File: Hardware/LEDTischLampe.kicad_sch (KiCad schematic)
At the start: 33 parts, among them J1 Conn_01x02_Socket, J2 USB_C_Receptacle_USB2.0_14P, J3 Conn_02x03_Counter_Clockwise, Q1 P-CHANNEL-MOSFET, SW1 Reset, SW2 User, U1 ESP32-C3-WROOM-02, U7 RY8310

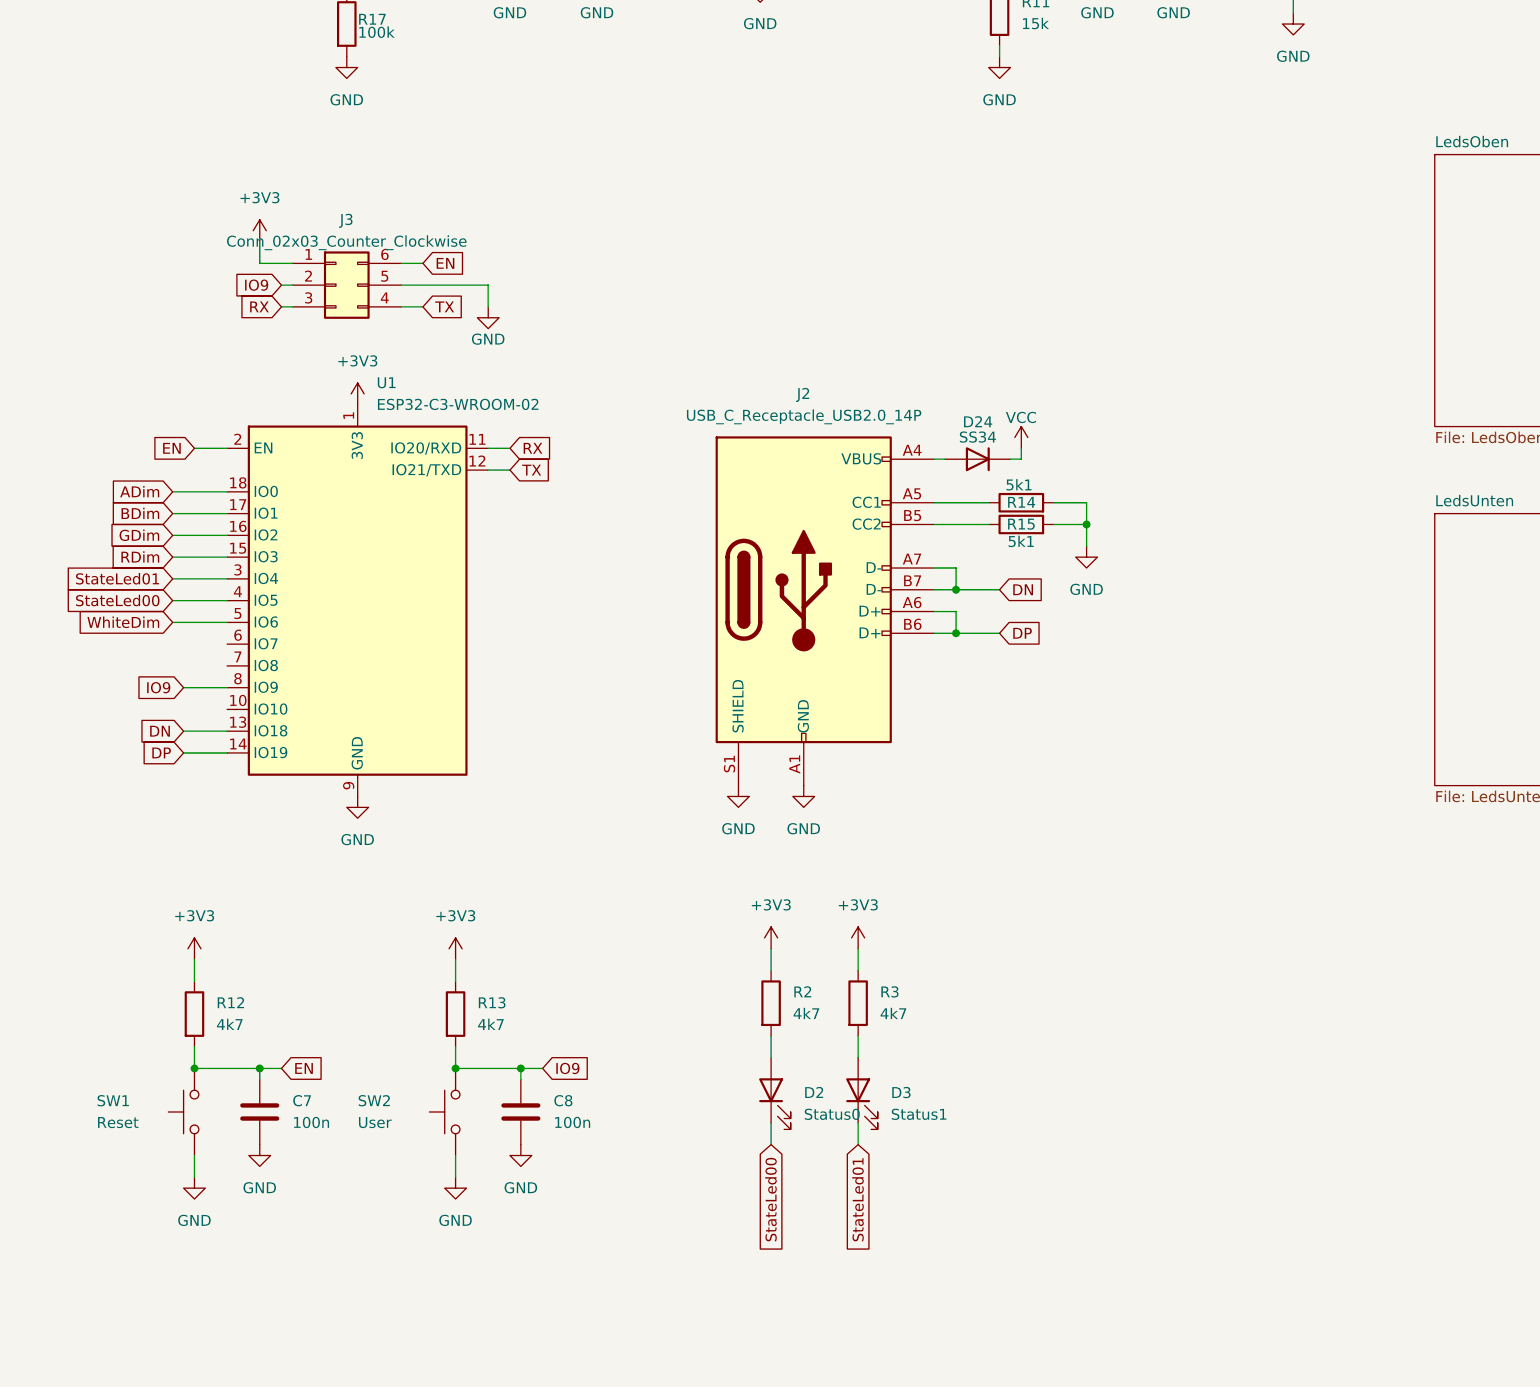
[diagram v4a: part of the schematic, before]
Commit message: some fixes and BOM optimization, heatsinking, etc
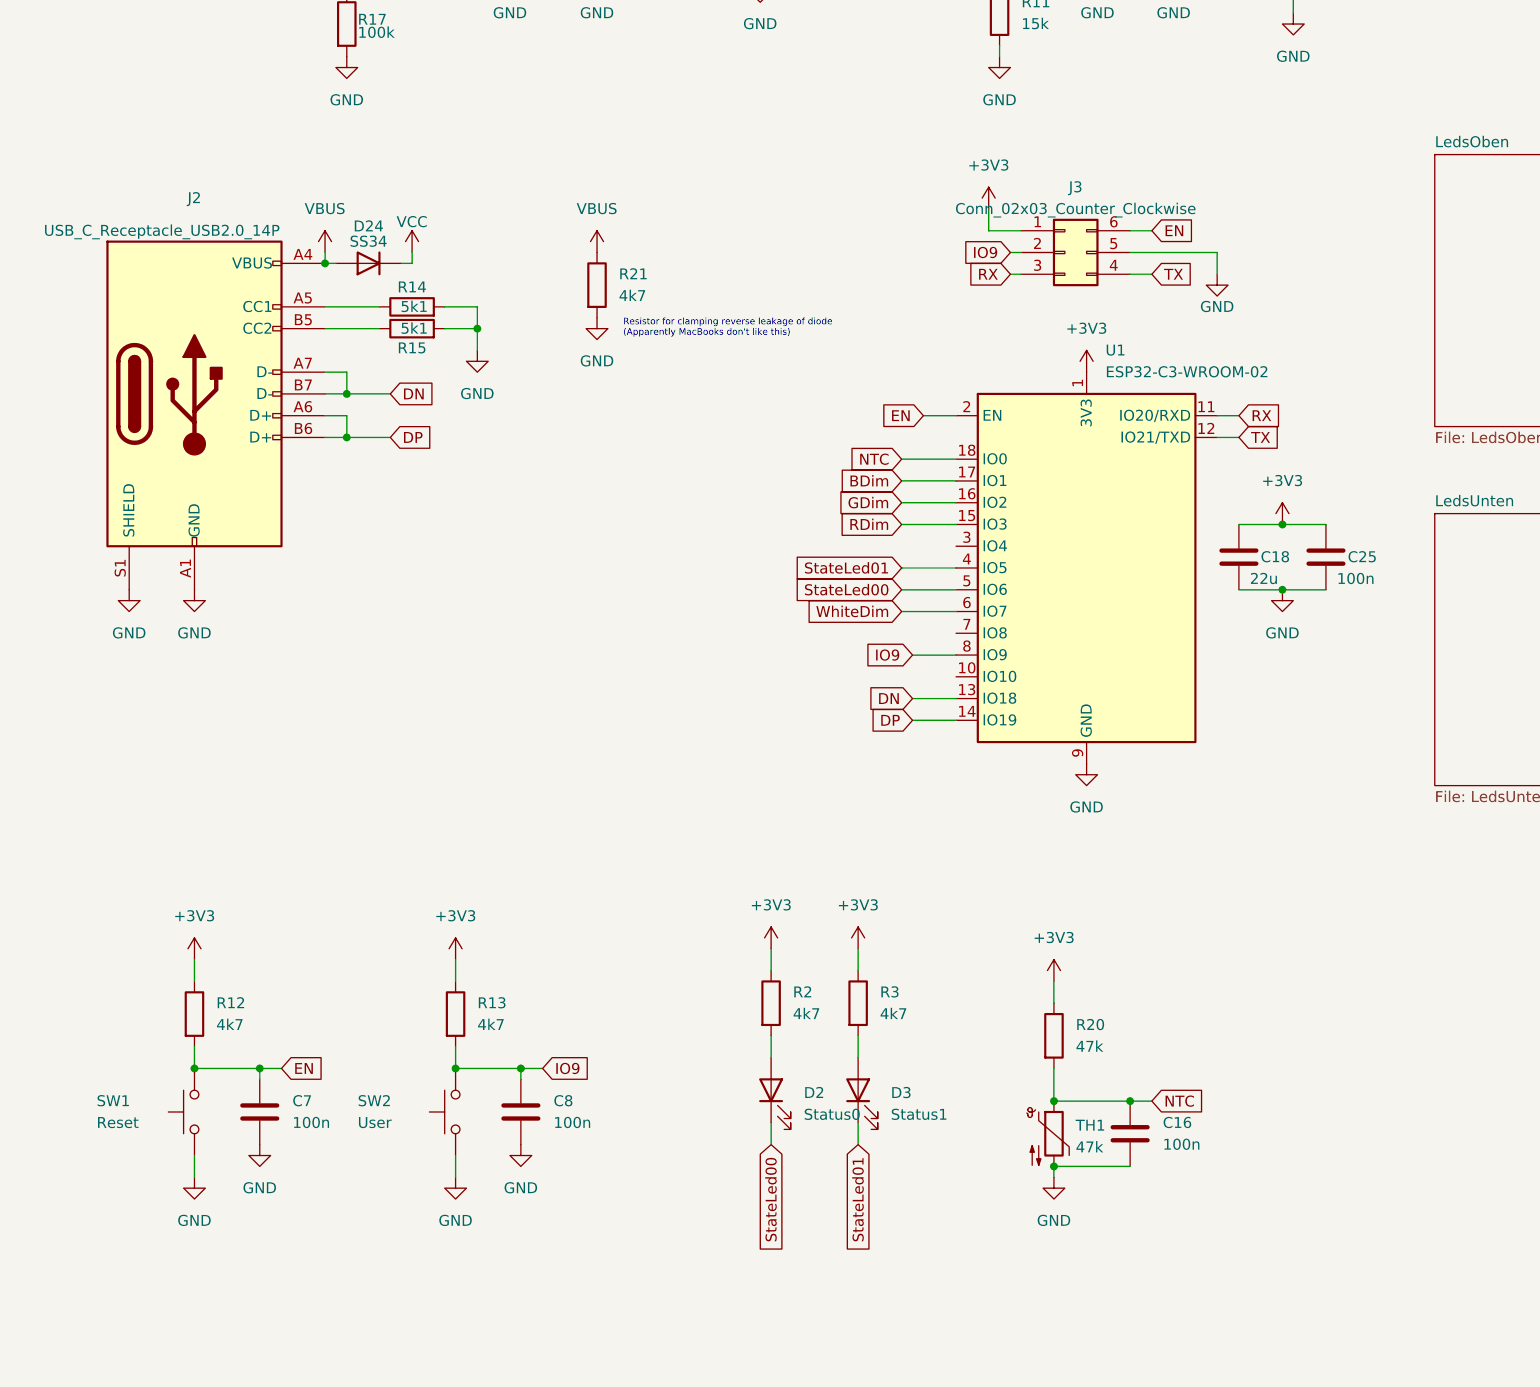
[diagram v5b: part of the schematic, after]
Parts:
- added C16, C25: 100n, Capacitor_SMD:C_0402_1005Metric, symbol Device:C
- added C18: 22u, Capacitor_SMD:C_1210_3225Metric, symbol Device:C
- added R20: 47k, Resistor_SMD:R_0402_1005Metric, symbol Device:R
- added R21: 4k7, Resistor_SMD:R_0402_1005Metric, symbol Device:R
- added TH1: 47k, Resistor_SMD:R_0402_1005Metric, symbol Device:Thermistor_NTC
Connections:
- net +3V3: now also C18.1, C25.1, R20.1
- net GND: now also C16.2, C18.2, C25.2, R21.2, TH1.2
- net StateLed00: now also U1.5 (IO6); no longer U1.4 (IO5)
- net StateLed01: now also U1.4 (IO5); no longer U1.3 (IO4)
- net WhiteDim: now also U1.6 (IO7); no longer U1.5 (IO6)
- net VBUS: now reaches D24.2 (A), J2.A4 (VBUS), J2.A9 (VBUS), J2.B4 (VBUS), J2.B9 (VBUS)
- net VBUS: now also R21.1
- net ADim renamed NTC
- net NTC: now also C16.1, R20.2, TH1.1
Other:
- note added: "Resistor for clamping reverse leakage of diode (Apparently MacBooks don't like this)"
- moved on the sheet: D24, J2, J3, R14, R15, U1

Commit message: final touches for v1.0
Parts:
- removed D34: 15V, Diode_SMD:D_0402_1005Metric, symbol Device:D_Zener
- removed Q1: P-CHANNEL-MOSFET, Package_SON:VSON-8_3.3x3.3mm_P0.65mm_NexFET, symbol Techbeard:P-CHANNEL-MOSFET
- removed R17: 100k, Resistor_SMD:R_0402_1005Metric, symbol Device:R
- added D25: SS34, Diode_SMD:D_SMA, symbol Device:D
- C1, C16, C25, C4, C5, C7, C8: LCSC C307331 -> (none)
- C18, C2, C6: footprint Capacitor_SMD:C_1210_3225Metric -> Capacitor_SMD:C_0805_2012Metric; LCSC C52306 -> (none)
- D1: LCSC C84256 -> (none)
- D2: LCSC C2296 -> (none)
- D24: LCSC C8678 -> (none)
- D3: LCSC C2297 -> (none)
- J2: LCSC C2927038 -> (none)
- L1: LCSC C5832376 -> (none)
- R1, R12, R13, R2, R20, R21, R3: LCSC C25900 -> (none)
- R10: LCSC C25792 -> (none)
- R11: LCSC C25756 -> (none)
- R14, R15: LCSC C25905 -> (none)
- SW1, SW2: LCSC C318884 -> (none)
- TH1: LCSC C2991699 -> (none)
- U1: LCSC C2934560 -> (none)
- U7: LCSC C370876 -> (none)
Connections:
- net GND: now also D25.2 (A)
- net VCC: now also J1.1 (Pin_1), D25.1 (K)
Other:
- note added: "Crowbar diode"

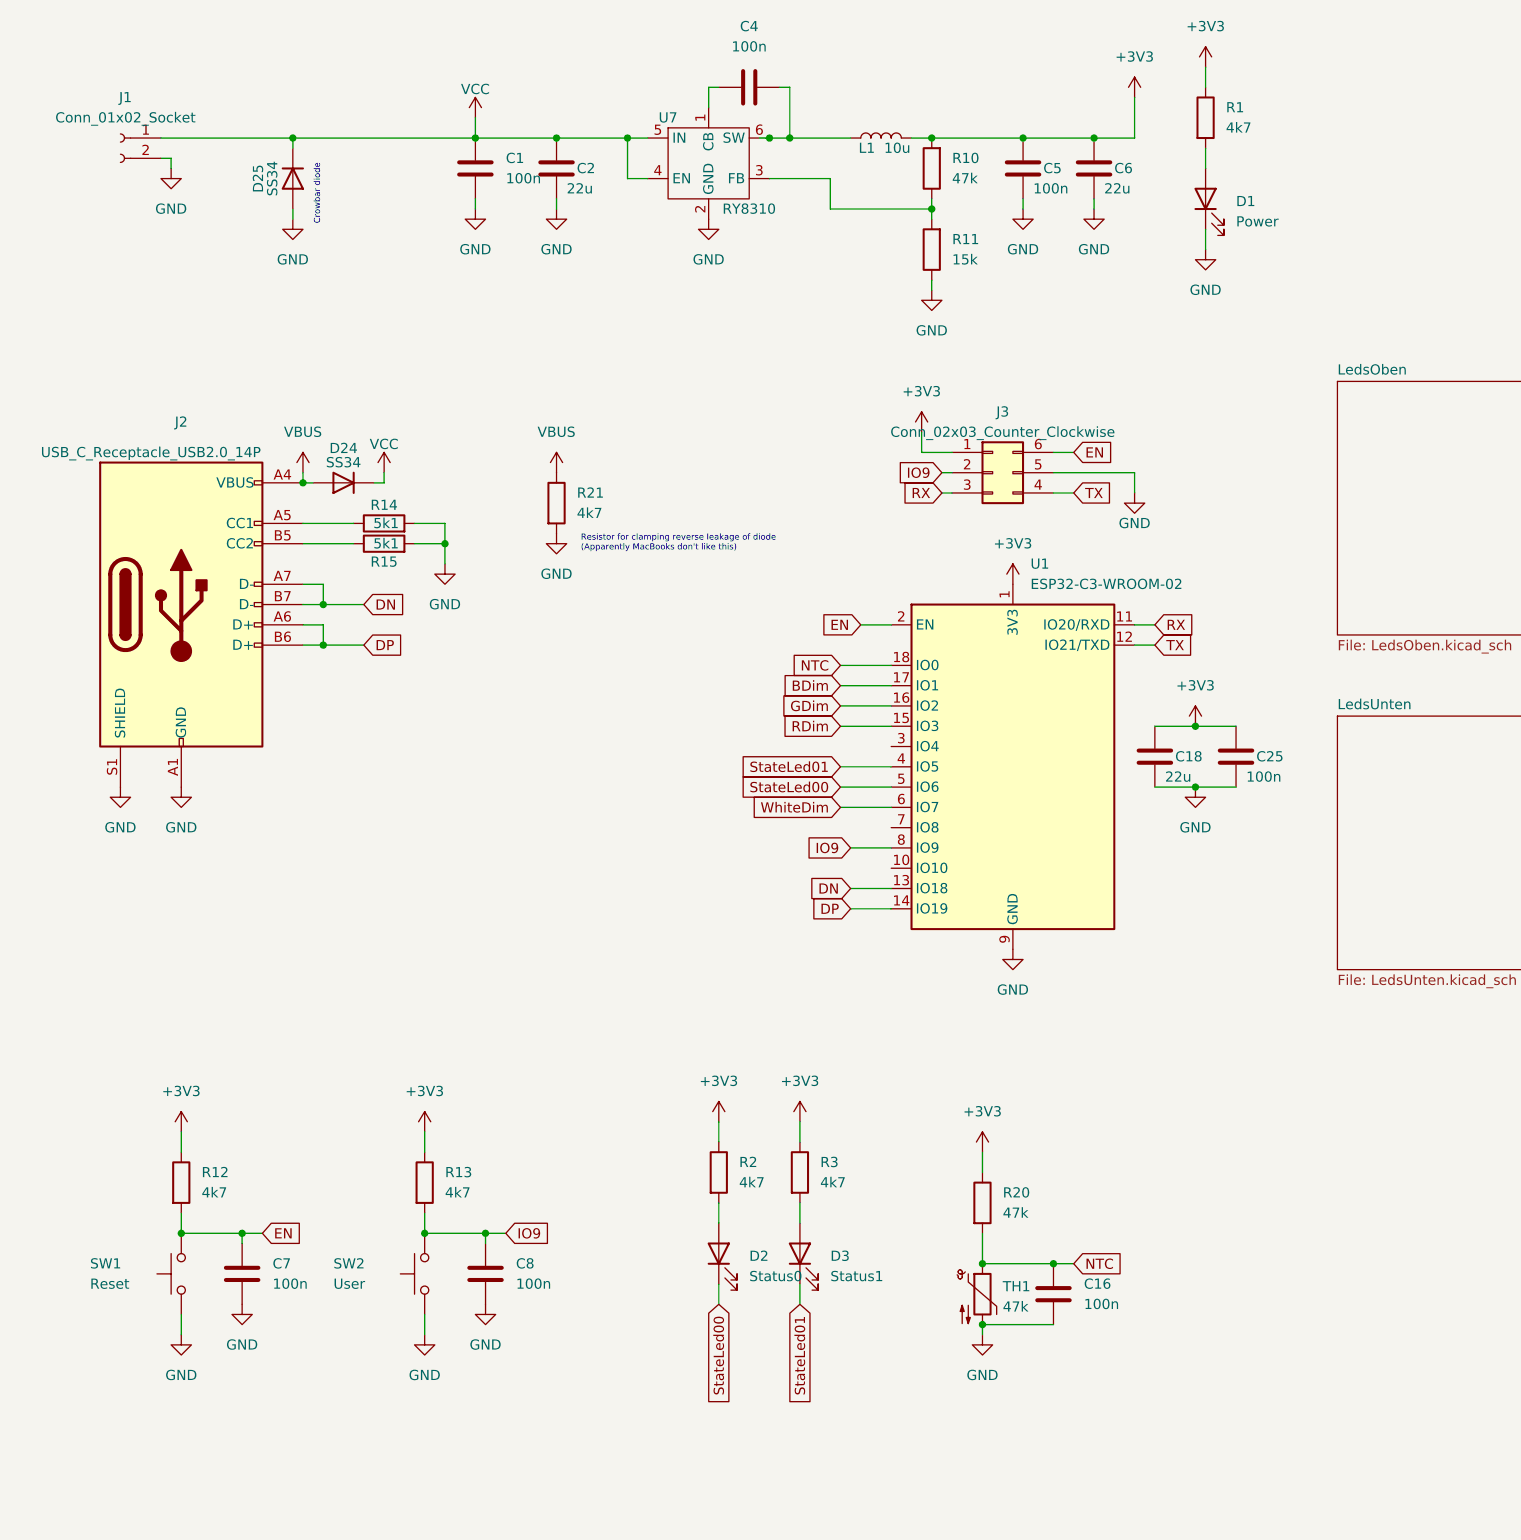
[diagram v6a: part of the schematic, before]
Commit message: some more tweaks (rotated input terminal block, added voltage measurement)
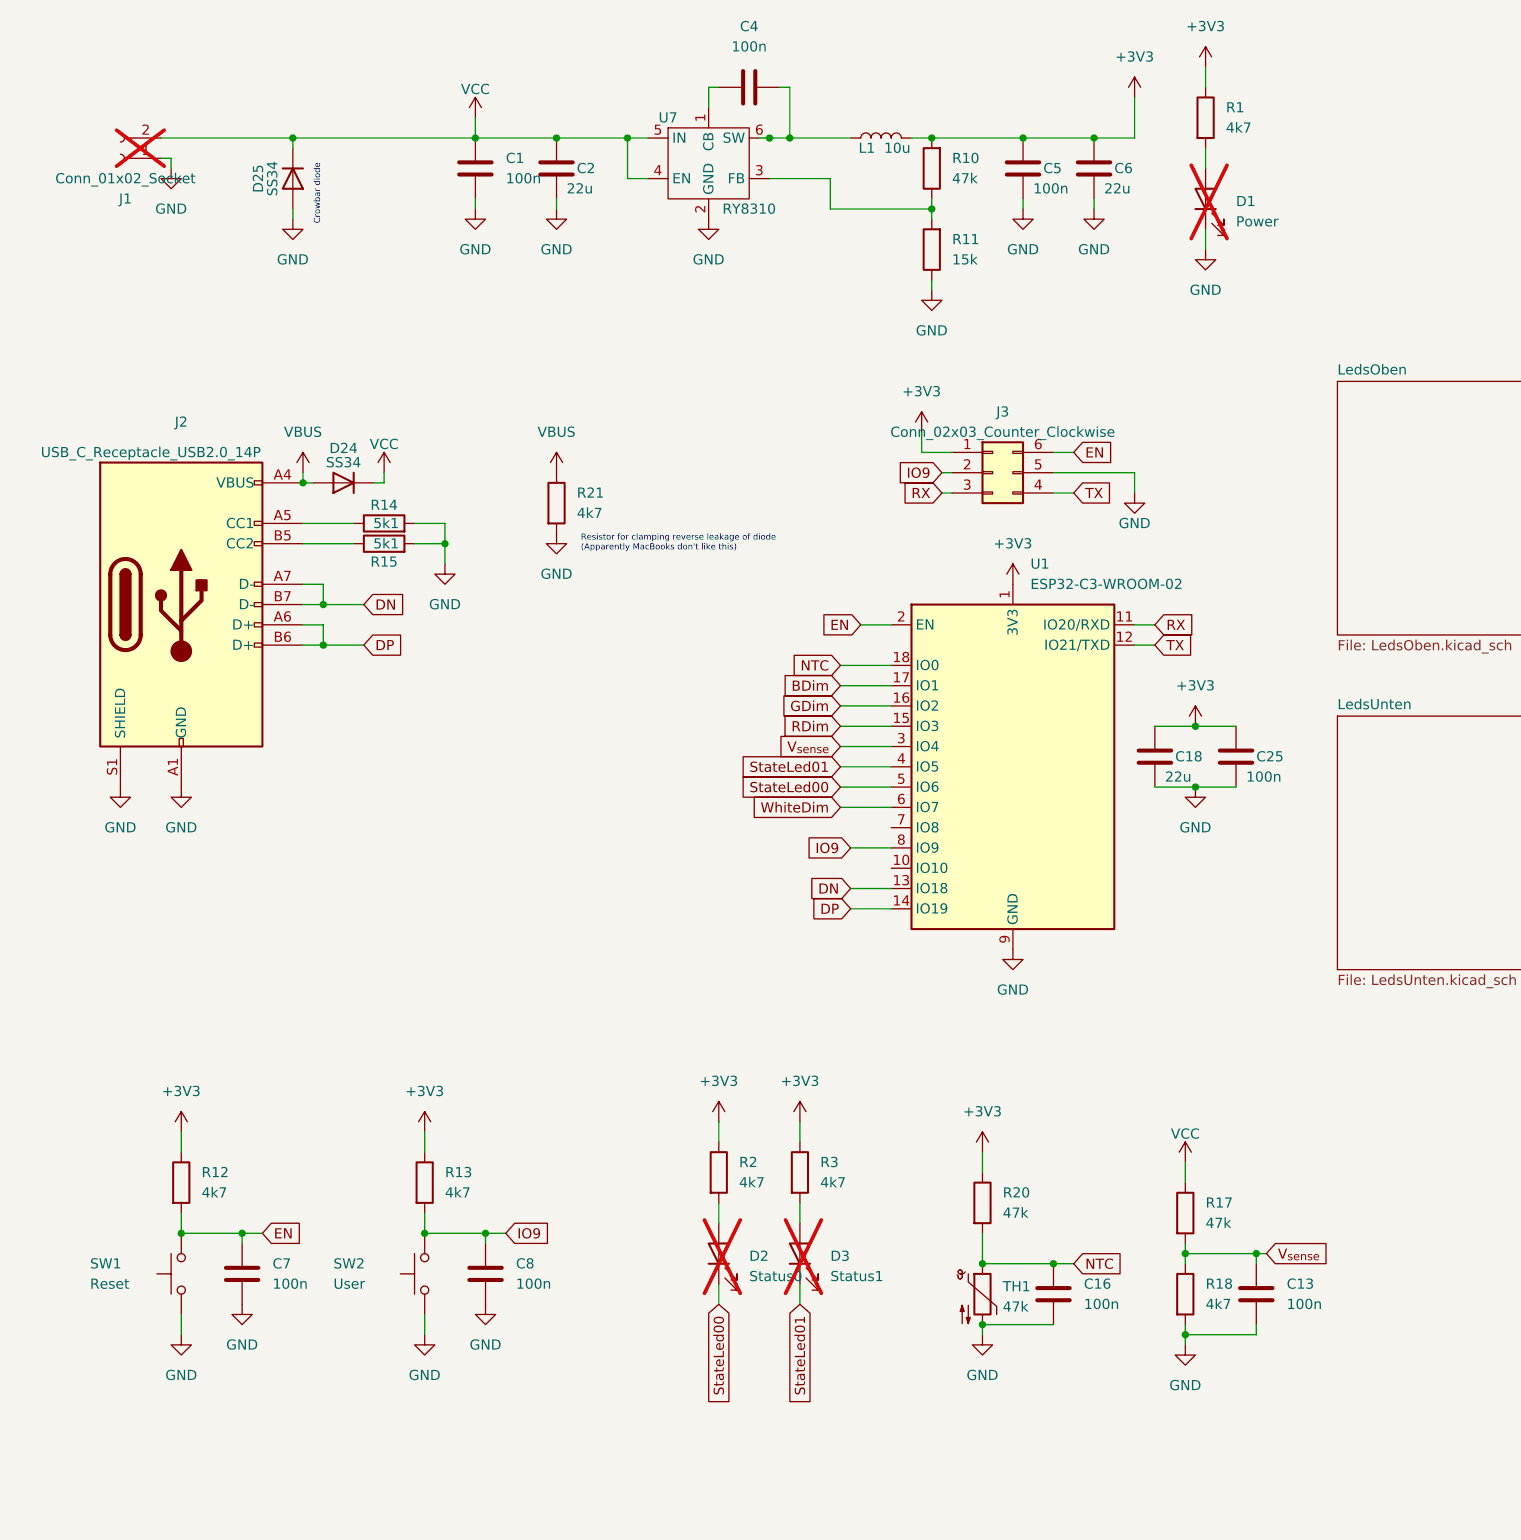
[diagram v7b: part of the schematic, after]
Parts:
- added C13: 100n, Capacitor_SMD:C_0402_1005Metric, symbol Device:C
- added R17: 47k, Resistor_SMD:R_0402_1005Metric, symbol Device:R
- added R18: 4k7, Resistor_SMD:R_0402_1005Metric, symbol Device:R
- D1, D2, D3, J1: now not fitted; now left out of the parts list
- J3: now left out of the parts list
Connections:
- net GND: now also J1.1 (Pin_1), C13.2, R18.2; no longer J1.2 (Pin_2)
- net VCC: now also J1.2 (Pin_2), R17.1; no longer J1.1 (Pin_1)
- net V_{sense}: now reaches U1.3 (IO4)
- net V_{sense}: now also C13.1, R17.2, R18.1
